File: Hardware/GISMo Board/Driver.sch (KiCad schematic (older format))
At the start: 13 parts, among them M0 M+, M1 M-, U1 DRV8876RGTR

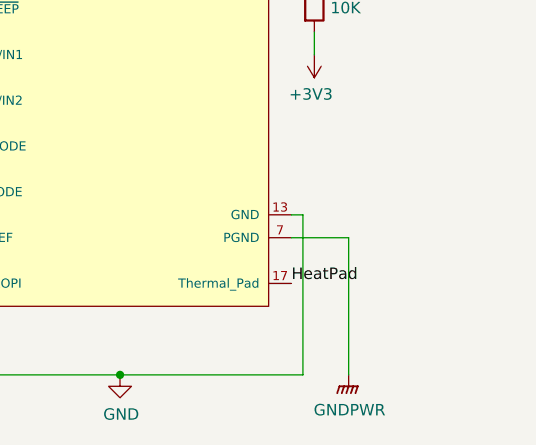
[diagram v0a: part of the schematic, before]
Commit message: Added head sink for motor driver
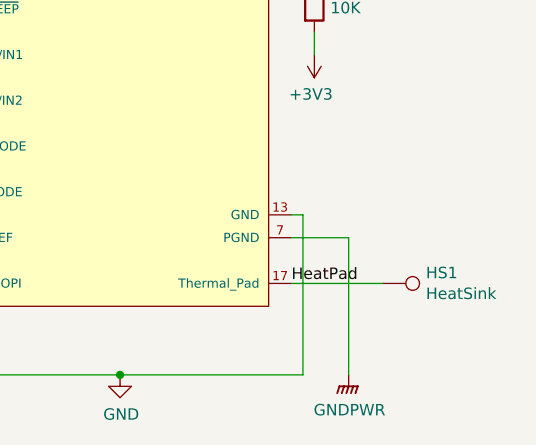
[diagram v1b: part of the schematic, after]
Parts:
- added HS1: HeatSink, TestPoint:TestPoint_Pad_2.0x2.0mm, symbol Connector:TestPoint
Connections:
- net HeatPad: now also HS1.1
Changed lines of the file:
@@
 Text Label 6800 4900 0    50   ~ 0
 HeatPad
+Wire Wire Line
+	6800 4900 7200 4900
+$Comp
+L Connector:TestPoint HS1
+U 1 1 5F5E89A5
+P 7200 4900
+F 0 "HS1" V 7154 5088 50  0000 L CNN
+F 1 "HeatSink" V 7245 5088 50  0000 L CNN
+F 2 "TestPoint:TestPoint_Pad_2.0x2.0mm" H 7400 4900 50  0001 C CNN
+F 3 "~" H 7400 4900 50  0001 C CNN
+	1    7200 4900
+	0    1    1    0
+$EndComp
 $EndSCHEMATC
